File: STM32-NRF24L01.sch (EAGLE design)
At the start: 5 parts, among them IC1 STM32F030K6T6

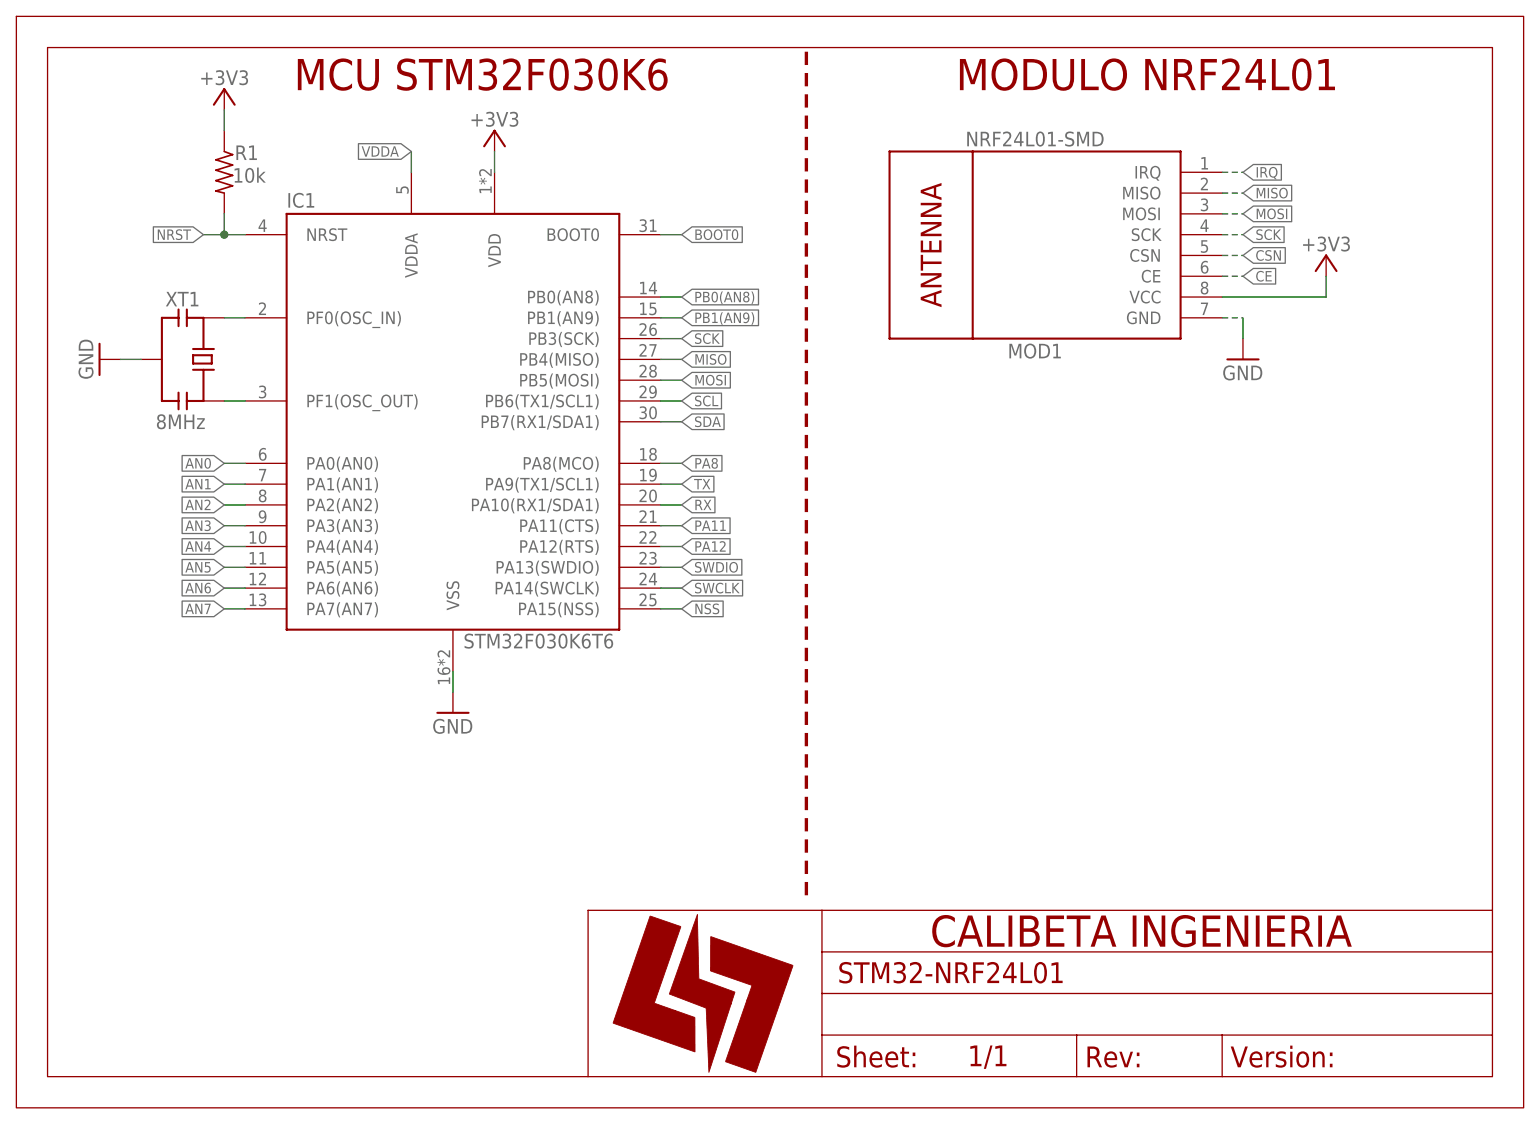
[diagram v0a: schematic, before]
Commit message: Add conectores y circuiteria basica para el STM32
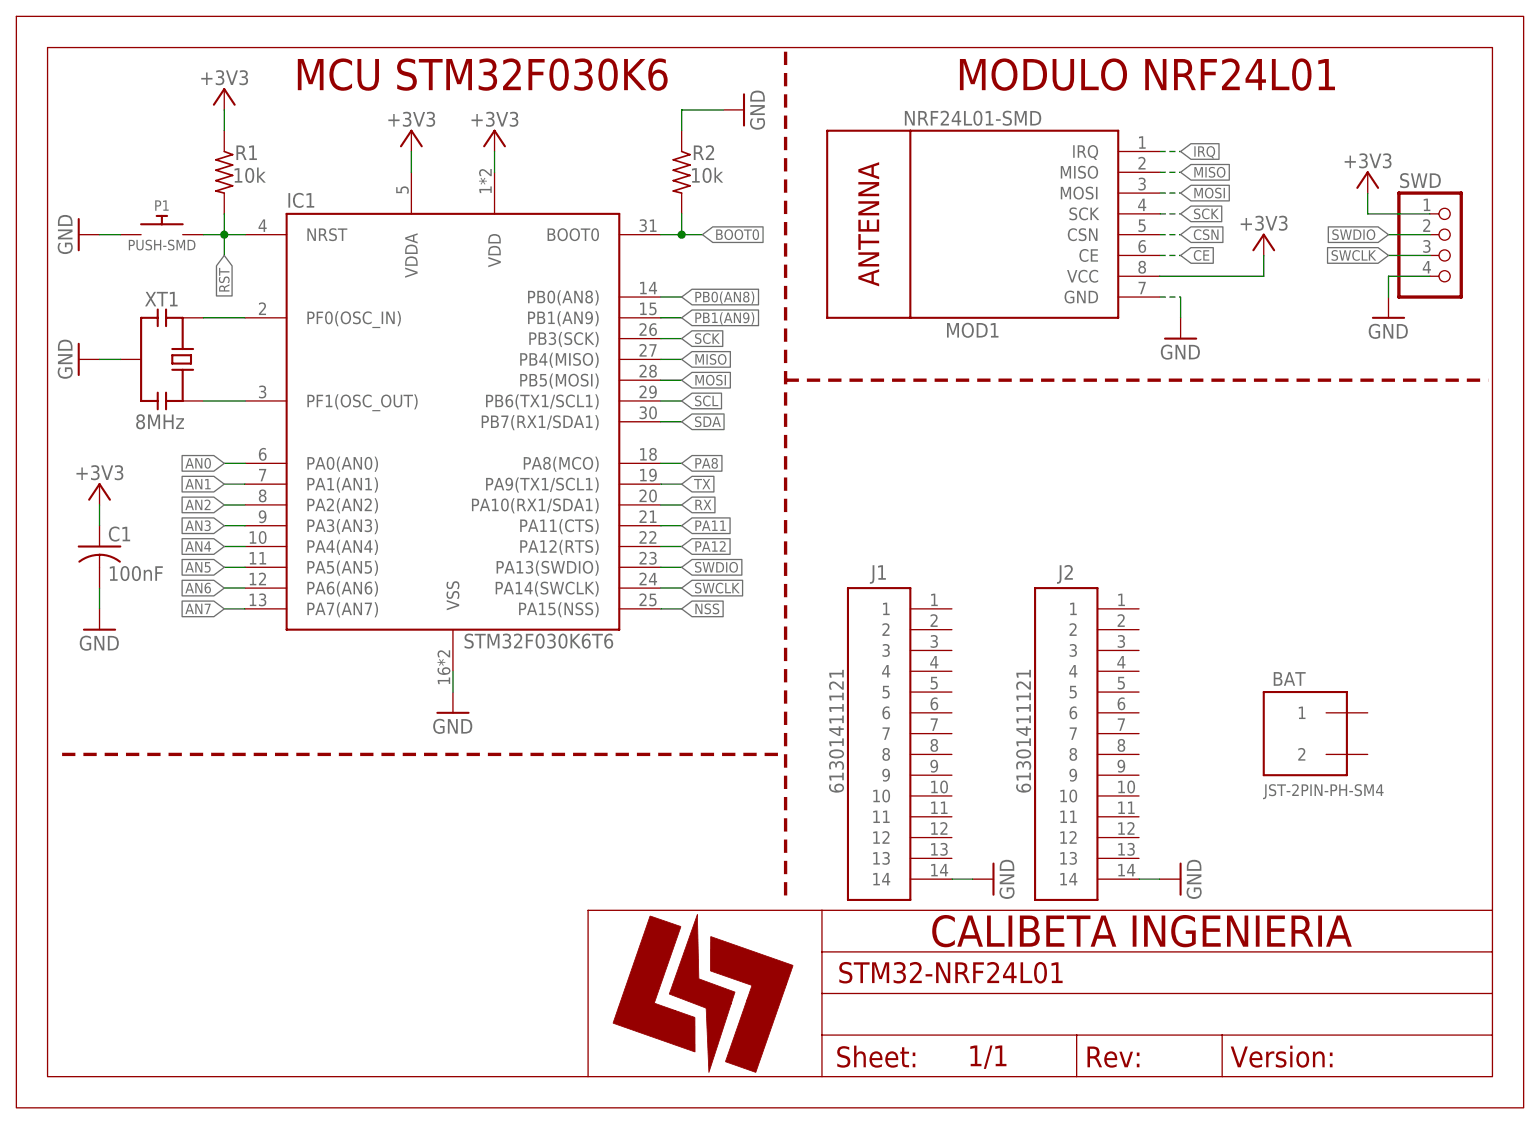
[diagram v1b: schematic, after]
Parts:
- added BAT: JST-2PIN-PH-SM4, CaliBeta-Conectores:JST-2PIN-PH-SM4
- added C1: 100nF, CaliBeta-RCL:CAPC0805
- added J1, J2: 61301411121, Headers:61301411121
- added P1: PUSH-SMD, CaliBeta-Miselaneos:PULSADOR-SMD-6035
- added R2: 10k, CaliBeta-RCL:RESISTOR_R0805
- added SWD: (no value), pinhead:PINHD-1X4/90
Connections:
- removed net NRST: IC1.NRST, R1.2
- removed net VDDA: IC1.VDDA
- new net RST: IC1.NRST, P1.2, R1.2
- net +3V3: now also C1.1, IC1.VDDA, SWD.1
- net BOOT0: now also R2.2
- net GND: now also C1.2, J1.14, J2.14, P1.1, R2.1, SWD.4
- net SWCLK: now also SWD.3
- net SWDIO: now also SWD.2
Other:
- moved on the sheet: MOD1, XT1

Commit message: Add cargador de bateria
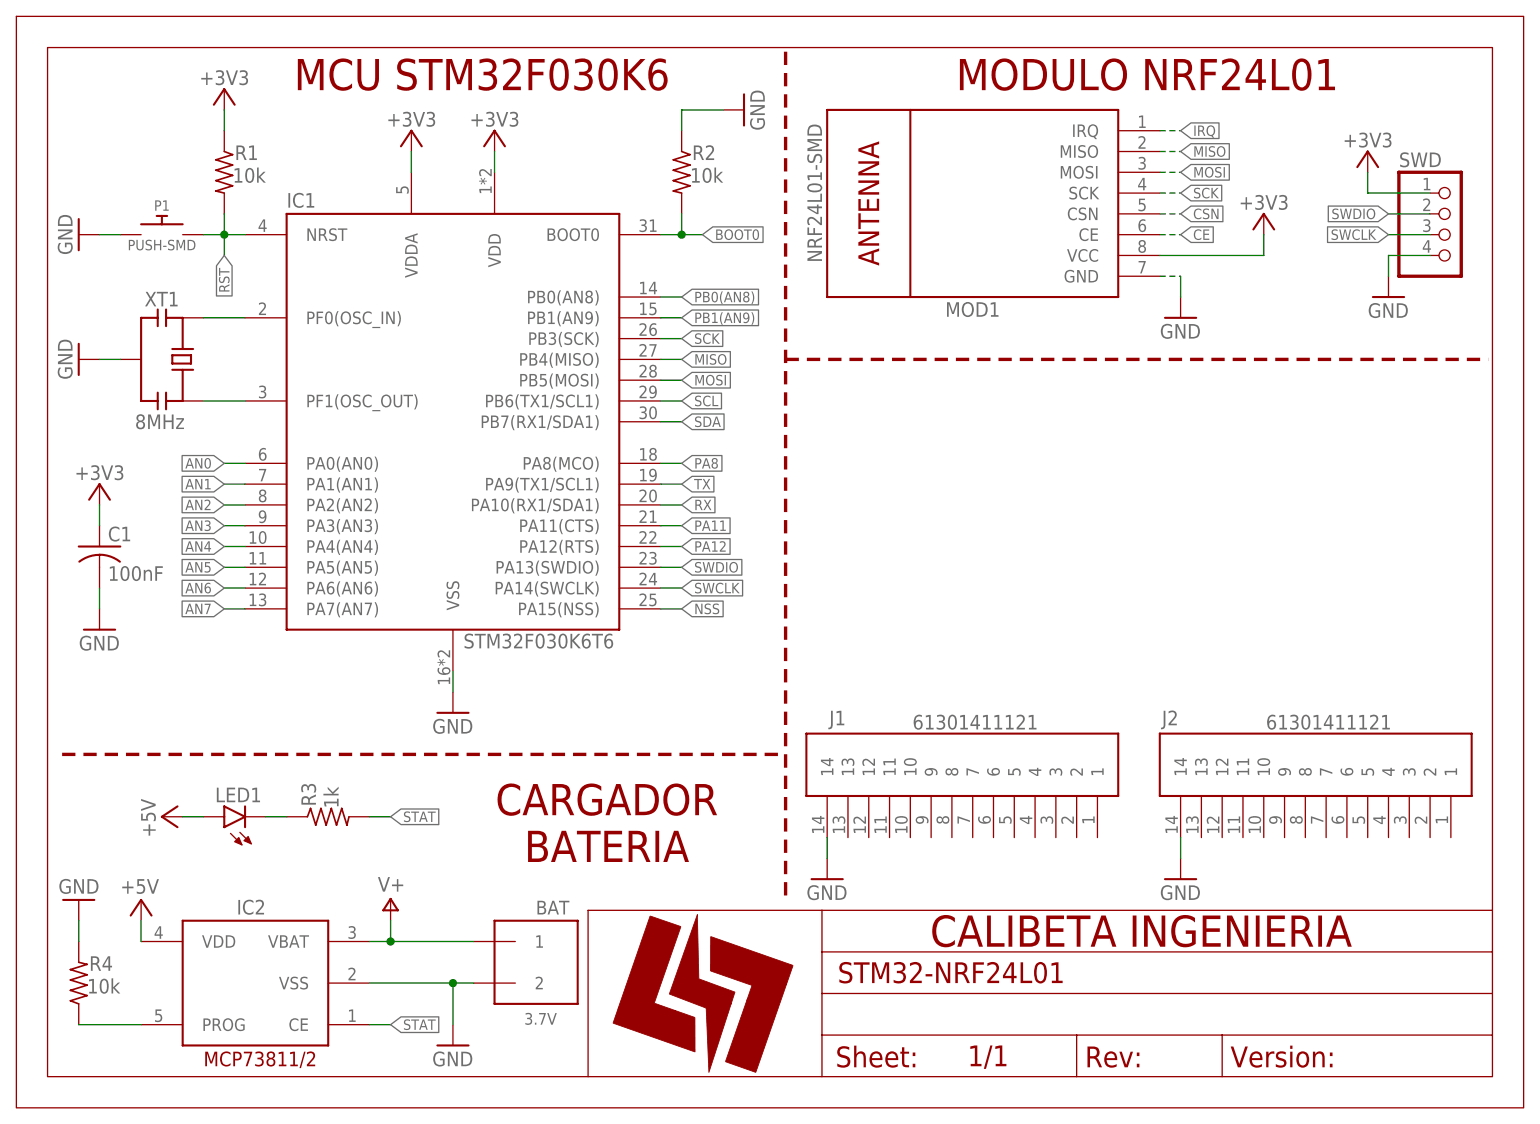
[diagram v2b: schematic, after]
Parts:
- added IC2: MCP73811/2, adafruit:MCP73811/2
- added LED1: (no value), CaliBeta-Diodos:LED-ROJO0805
- added R3: 1k, CaliBeta-RCL:RESISTOR_R0805
- added R4: 10k, CaliBeta-RCL:RESISTOR_R0805
- BAT: value JST-2PIN-PH-SM4 -> 3.7V
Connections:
- new net +5V: IC2.VDD, LED1.A
- new net N$7: LED1.C, R3.1
- new net N$8: IC2.PROG, R4.1
- new net STAT: IC2.CE, R3.2
- new net V+: BAT.1, IC2.VBAT
- net GND: now also BAT.2, IC2.VSS, R4.2
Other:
- note added: "CARGADOR BATERIA"
- moved on the sheet: BAT, J1, J2, MOD1, SWD
